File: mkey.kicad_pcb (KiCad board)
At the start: 2 copper layers, 1 part, among them U1 ESP32-S3-WROOM-2

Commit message: Initial KLE import of layout, need to add stabs and other sized keys
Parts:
- added BOOT_SW1: SW_Push, Connector_USB:USB_C_Receptacle_HRO_TYPE-C-31-M-12, F.Cu at (336.1, -28.6)
- added C1: 1uF 16V, Capacitor_SMD:C_0402_1005Metric, F.Cu at (346.3, -33.4)
- added C2: 10uF 16V, Capacitor_SMD:C_0805_2012Metric, F.Cu at (346.3, -31.4)
- added C3: 22pF 50V, Capacitor_SMD:C_0603_1608Metric, F.Cu at (346.3, -29.5)
- added C4: 10uF 16V, Capacitor_SMD:C_0805_2012Metric, F.Cu at (346.3, -27.5)
- added C5: 1uF 16V, Capacitor_SMD:C_0402_1005Metric, F.Cu at (350.0, -22.6)
- added C6: 100nF 10V, Capacitor_SMD:C_0402_1005Metric, F.Cu at (355.9, -23.9)
- added C7: 10nF 10V, Capacitor_SMD:C_0402_1005Metric, F.Cu at (350.0, -19.6)
- added C8: 1nF 10V, Capacitor_SMD:C_0402_1005Metric, F.Cu at (346.3, -25.5)
- added D1: D_Small, Diode_SMD:D_SOD-123, F.Cu at (50.0, 59.5)
- added D10: D_Small, Diode_SMD:D_SOD-123, F.Cu at (221.5, 59.5)
- added D11: D_Small, Diode_SMD:D_SOD-123, F.Cu at (240.5, 59.5)
- added D12: D_Small, Diode_SMD:D_SOD-123, F.Cu at (259.6, 59.5)
- added D13: D_Small, Diode_SMD:D_SOD-123, F.Cu at (278.6, 59.5)
- added D14: D_Small, Diode_SMD:D_SOD-123, F.Cu at (307.2, 59.5)
- added D15: D_Small, Diode_SMD:D_SOD-123, F.Cu at (54.8, 78.5)
- added D16: D_Small, Diode_SMD:D_SOD-123, F.Cu at (78.6, 78.5)
- added D17: D_Small, Diode_SMD:D_SOD-123, F.Cu at (97.6, 78.5)
- added D18: D_Small, Diode_SMD:D_SOD-123, F.Cu at (116.7, 78.5)
- added D19: D_Small, Diode_SMD:D_SOD-123, F.Cu at (135.7, 78.5)
- added D2: D_Small, Diode_SMD:D_SOD-123, F.Cu at (69.1, 59.5)
- added D20: D_Small, Diode_SMD:D_SOD-123, F.Cu at (154.8, 78.5)
- added D21: D_Small, Diode_SMD:D_SOD-123, F.Cu at (173.8, 78.5)
- added D22: D_Small, Diode_SMD:D_SOD-123, F.Cu at (192.9, 78.5)
- added D23: D_Small, Diode_SMD:D_SOD-123, F.Cu at (211.9, 78.5)
- added D24: D_Small, Diode_SMD:D_SOD-123, F.Cu at (231.0, 78.5)
- added D25: D_Small, Diode_SMD:D_SOD-123, F.Cu at (250.0, 78.5)
- added D26: D_Small, Diode_SMD:D_SOD-123, F.Cu at (269.1, 78.5)
- added D27: D_Small, Diode_SMD:D_SOD-123, F.Cu at (288.1, 78.5)
- added D28: D_Small, Diode_SMD:D_SOD-123, F.Cu at (314.3, 88.0)
- added D29: D_Small, Diode_SMD:D_SOD-123, F.Cu at (57.1, 97.6)
- added D3: D_Small, Diode_SMD:D_SOD-123, F.Cu at (88.1, 59.5)
- added D30: D_Small, Diode_SMD:D_SOD-123, F.Cu at (83.3, 97.6)
- added D31: D_Small, Diode_SMD:D_SOD-123, F.Cu at (102.4, 97.6)
- added D32: D_Small, Diode_SMD:D_SOD-123, F.Cu at (121.4, 97.6)
- added D33: D_Small, Diode_SMD:D_SOD-123, F.Cu at (140.5, 97.6)
- added D34: D_Small, Diode_SMD:D_SOD-123, F.Cu at (159.5, 97.6)
- added D35: D_Small, Diode_SMD:D_SOD-123, F.Cu at (178.6, 97.6)
- added D36: D_Small, Diode_SMD:D_SOD-123, F.Cu at (197.6, 97.6)
- added D37: D_Small, Diode_SMD:D_SOD-123, F.Cu at (216.7, 97.6)
- added D38: D_Small, Diode_SMD:D_SOD-123, F.Cu at (235.7, 97.6)
- added D39: D_Small, Diode_SMD:D_SOD-123, F.Cu at (254.8, 97.6)
- added D4: D_Small, Diode_SMD:D_SOD-123, F.Cu at (107.2, 59.5)
- added D40: D_Small, Diode_SMD:D_SOD-123, F.Cu at (273.8, 97.6)
- added D41: D_Small, Diode_SMD:D_SOD-123, F.Cu at (292.9, 97.6)
- added D42: D_Small, Diode_SMD:D_SOD-123, F.Cu at (52.4, 116.6)
- added D43: D_Small, Diode_SMD:D_SOD-123, F.Cu at (73.8, 116.6)
- added D44: D_Small, Diode_SMD:D_SOD-123, F.Cu at (92.9, 116.6)
- added D45: D_Small, Diode_SMD:D_SOD-123, F.Cu at (111.9, 116.6)
- added D46: D_Small, Diode_SMD:D_SOD-123, F.Cu at (131.0, 116.6)
- added D47: D_Small, Diode_SMD:D_SOD-123, F.Cu at (150.0, 116.6)
- added D48: D_Small, Diode_SMD:D_SOD-123, F.Cu at (169.1, 116.6)
- added D49: D_Small, Diode_SMD:D_SOD-123, F.Cu at (188.1, 116.6)
- added D5: D_Small, Diode_SMD:D_SOD-123, F.Cu at (126.2, 59.5)
- added D50: D_Small, Diode_SMD:D_SOD-123, F.Cu at (207.2, 116.6)
- added D51: D_Small, Diode_SMD:D_SOD-123, F.Cu at (226.2, 116.6)
- added D52: D_Small, Diode_SMD:D_SOD-123, F.Cu at (245.3, 116.6)
- added D53: D_Small, Diode_SMD:D_SOD-123, F.Cu at (264.3, 116.6)
- added D54: D_Small, Diode_SMD:D_SOD-123, F.Cu at (300.0, 116.6)
- added D55: D_Small, Diode_SMD:D_SOD-123, F.Cu at (359.6, 116.6)
- added D56: D_Small, Diode_SMD:D_SOD-123, F.Cu at (52.4, 135.7)
- added D57: D_Small, Diode_SMD:D_SOD-123, F.Cu at (76.2, 135.7)
- added D58: D_Small, Diode_SMD:D_SOD-123, F.Cu at (100.0, 135.7)
- added D59: D_Small, Diode_SMD:D_SOD-123, F.Cu at (171.4, 135.7)
- added D6: D_Small, Diode_SMD:D_SOD-123, F.Cu at (145.3, 59.5)
- added D60: D_Small, Diode_SMD:D_SOD-123, F.Cu at (242.9, 135.7)
- added D61: D_Small, Diode_SMD:D_SOD-123, F.Cu at (266.7, 135.7)
- added D62: D_Small, Diode_SMD:D_SOD-123, F.Cu at (290.5, 135.7)
- added D63: D_Small, Diode_SMD:D_SOD-123, F.Cu at (314.3, 135.7)
- added D64: D_Small, Diode_SMD:D_SOD-123, F.Cu at (340.5, 135.7)
- added D65: D_Small, Diode_SMD:D_SOD-123, F.Cu at (359.6, 135.7)
- added D66: D_Small, Diode_SMD:D_SOD-123, F.Cu at (378.6, 135.7)
- added D67: B5819W, Diode_SMD:D_SOD-123, F.Cu at (362.2, -56.2)
- added D68: PESD3V3L1BA,115, Diode_SMD:D_SOD-323, F.Cu at (362.2, -52.8)
- added D69: SP0503BAHT, Package_TO_SOT_SMD:SOT-143, B.Cu at (276.2, 60.0)
- added D7: D_Small, Diode_SMD:D_SOD-123, F.Cu at (164.3, 59.5)
- added D8: D_Small, Diode_SMD:D_SOD-123, F.Cu at (183.4, 59.5)
- added D9: D_Small, Diode_SMD:D_SOD-123, F.Cu at (202.4, 59.5)
- added J1: USB_C_REP_2.0, Connector_USB:USB_C_Receptacle_HRO_TYPE-C-31-M-12, F.Cu at (336.1, -18.1)
- added L1: SPH4018H2R2MT (2.2uH 2.2A), Inductor_SMD:L_Bourns-SRN4018, F.Cu at (350.8, -26.9)
- added MX1: MX_SW_solder, PCM_marbastlib-mx:SW_MX_1u, F.Cu at (46.8, 58.7)
- added MX10: MX_SW_solder, PCM_marbastlib-mx:SW_MX_1u, F.Cu at (218.3, 58.7)
- added MX11: MX_SW_solder, PCM_marbastlib-mx:SW_MX_1u, F.Cu at (237.3, 58.7)
- added MX12: MX_SW_solder, PCM_marbastlib-mx:SW_MX_1u, F.Cu at (256.4, 58.7)
- added MX13: MX_SW_solder, PCM_marbastlib-mx:SW_MX_1u, F.Cu at (275.4, 58.7)
- added MX14: MX_SW_solder, PCM_marbastlib-mx:SW_MX_1u, F.Cu at (304.0, 58.7)
- added MX15: MX_SW_solder, PCM_marbastlib-mx:SW_MX_1u, F.Cu at (51.6, 77.7)
- added MX16: MX_SW_solder, PCM_marbastlib-mx:SW_MX_1u, F.Cu at (75.4, 77.7)
- added MX17: MX_SW_solder, PCM_marbastlib-mx:SW_MX_1u, F.Cu at (94.5, 77.7)
- added MX18: MX_SW_solder, PCM_marbastlib-mx:SW_MX_1u, F.Cu at (113.5, 77.7)
- added MX19: MX_SW_solder, PCM_marbastlib-mx:SW_MX_1u, F.Cu at (132.6, 77.7)
- added MX2: MX_SW_solder, PCM_marbastlib-mx:SW_MX_1u, F.Cu at (65.9, 58.7)
- added MX20: MX_SW_solder, PCM_marbastlib-mx:SW_MX_1u, F.Cu at (151.6, 77.7)
- added MX21: MX_SW_solder, PCM_marbastlib-mx:SW_MX_1u, F.Cu at (170.7, 77.7)
- added MX22: MX_SW_solder, PCM_marbastlib-mx:SW_MX_1u, F.Cu at (189.7, 77.7)
- added MX23: MX_SW_solder, PCM_marbastlib-mx:SW_MX_1u, F.Cu at (208.8, 77.7)
- added MX24: MX_SW_solder, PCM_marbastlib-mx:SW_MX_1u, F.Cu at (227.8, 77.7)
- added MX25: MX_SW_solder, PCM_marbastlib-mx:SW_MX_1u, F.Cu at (246.9, 77.7)
- added MX26: MX_SW_solder, PCM_marbastlib-mx:SW_MX_1u, F.Cu at (265.9, 77.7)
- added MX27: MX_SW_solder, PCM_marbastlib-mx:SW_MX_1u, F.Cu at (285.0, 77.7)
- added MX28: MX_SW_solder, PCM_marbastlib-mx:SW_MX_1u, F.Cu at (311.1, 87.2)
- added MX29: MX_SW_solder, PCM_marbastlib-mx:SW_MX_1u, F.Cu at (54.0, 96.8)
- added MX3: MX_SW_solder, PCM_marbastlib-mx:SW_MX_1u, F.Cu at (84.9, 58.7)
- added MX30: MX_SW_solder, PCM_marbastlib-mx:SW_MX_1u, F.Cu at (80.2, 96.8)
- added MX31: MX_SW_solder, PCM_marbastlib-mx:SW_MX_1u, F.Cu at (99.2, 96.8)
- added MX32: MX_SW_solder, PCM_marbastlib-mx:SW_MX_1u, F.Cu at (118.3, 96.8)
- added MX33: MX_SW_solder, PCM_marbastlib-mx:SW_MX_1u, F.Cu at (137.3, 96.8)
- added MX34: MX_SW_solder, PCM_marbastlib-mx:SW_MX_1u, F.Cu at (156.4, 96.8)
- added MX35: MX_SW_solder, PCM_marbastlib-mx:SW_MX_1u, F.Cu at (175.4, 96.8)
- added MX36: MX_SW_solder, PCM_marbastlib-mx:SW_MX_1u, F.Cu at (194.5, 96.8)
- added MX37: MX_SW_solder, PCM_marbastlib-mx:SW_MX_1u, F.Cu at (213.5, 96.8)
- added MX38: MX_SW_solder, PCM_marbastlib-mx:SW_MX_1u, F.Cu at (232.6, 96.8)
- added MX39: MX_SW_solder, PCM_marbastlib-mx:SW_MX_1u, F.Cu at (251.6, 96.8)
- added MX4: MX_SW_solder, PCM_marbastlib-mx:SW_MX_1u, F.Cu at (104.0, 58.7)
- added MX40: MX_SW_solder, PCM_marbastlib-mx:SW_MX_1u, F.Cu at (270.7, 96.8)
- added MX41: MX_SW_solder, PCM_marbastlib-mx:SW_MX_1u, F.Cu at (289.7, 96.8)
- added MX42: MX_SW_solder, PCM_marbastlib-mx:SW_MX_1u, F.Cu at (49.2, 115.8)
- added MX43: MX_SW_solder, PCM_marbastlib-mx:SW_MX_1u, F.Cu at (70.6, 115.8)
- added MX44: MX_SW_solder, PCM_marbastlib-mx:SW_MX_1u, F.Cu at (89.7, 115.8)
- added MX45: MX_SW_solder, PCM_marbastlib-mx:SW_MX_1u, F.Cu at (108.7, 115.8)
- added MX46: MX_SW_solder, PCM_marbastlib-mx:SW_MX_1u, F.Cu at (127.8, 115.8)
- added MX47: MX_SW_solder, PCM_marbastlib-mx:SW_MX_1u, F.Cu at (146.8, 115.8)
- added MX48: MX_SW_solder, PCM_marbastlib-mx:SW_MX_1u, F.Cu at (165.9, 115.8)
- added MX49: MX_SW_solder, PCM_marbastlib-mx:SW_MX_1u, F.Cu at (184.9, 115.8)
- added MX5: MX_SW_solder, PCM_marbastlib-mx:SW_MX_1u, F.Cu at (123.0, 58.7)
- added MX50: MX_SW_solder, PCM_marbastlib-mx:SW_MX_1u, F.Cu at (204.0, 115.8)
- added MX51: MX_SW_solder, PCM_marbastlib-mx:SW_MX_1u, F.Cu at (223.0, 115.8)
- added MX52: MX_SW_solder, PCM_marbastlib-mx:SW_MX_1u, F.Cu at (242.1, 115.8)
- added MX53: MX_SW_solder, PCM_marbastlib-mx:SW_MX_1u, F.Cu at (261.1, 115.8)
- added MX54: MX_SW_solder, PCM_marbastlib-mx:SW_MX_1u, F.Cu at (296.9, 115.8)
- added MX55: MX_SW_solder, PCM_marbastlib-mx:SW_MX_1u, F.Cu at (356.4, 115.8)
- added MX56: MX_SW_solder, PCM_marbastlib-mx:SW_MX_1u, F.Cu at (49.2, 134.9)
- added MX57: MX_SW_solder, PCM_marbastlib-mx:SW_MX_1u, F.Cu at (73.0, 134.9)
- added MX58: MX_SW_solder, PCM_marbastlib-mx:SW_MX_1u, F.Cu at (96.8, 134.9)
- added MX59: MX_SW_solder, PCM_marbastlib-mx:SW_MX_1u, F.Cu at (168.3, 134.9)
- added MX6: MX_SW_solder, PCM_marbastlib-mx:SW_MX_1u, F.Cu at (142.1, 58.7)
- added MX60: MX_SW_solder, PCM_marbastlib-mx:SW_MX_1u, F.Cu at (239.7, 134.9)
- added MX61: MX_SW_solder, PCM_marbastlib-mx:SW_MX_1u, F.Cu at (263.5, 134.9)
- added MX62: MX_SW_solder, PCM_marbastlib-mx:SW_MX_1u, F.Cu at (287.3, 134.9)
- added MX63: MX_SW_solder, PCM_marbastlib-mx:SW_MX_1u, F.Cu at (311.1, 134.9)
- added MX64: MX_SW_solder, PCM_marbastlib-mx:SW_MX_1u, F.Cu at (337.3, 134.9)
- added MX65: MX_SW_solder, PCM_marbastlib-mx:SW_MX_1u, F.Cu at (356.4, 134.9)
- added MX66: MX_SW_solder, PCM_marbastlib-mx:SW_MX_1u, F.Cu at (375.4, 134.9)
- added MX7: MX_SW_solder, PCM_marbastlib-mx:SW_MX_1u, F.Cu at (161.1, 58.7)
- added MX8: MX_SW_solder, PCM_marbastlib-mx:SW_MX_1u, F.Cu at (180.2, 58.7)
- added MX9: MX_SW_solder, PCM_marbastlib-mx:SW_MX_1u, F.Cu at (199.2, 58.7)
- added R1: 10kR 1%, Resistor_SMD:R_0402_1005Metric, F.Cu at (343.4, -33.4)
- added R2: 10kR 1%, Resistor_SMD:R_0402_1005Metric, F.Cu at (343.4, -31.4)
- added R3: 100kR 1%, Resistor_SMD:R_0402_1005Metric, F.Cu at (343.4, -29.4)
- added R4: 22k1R 1%, Resistor_SMD:R_0402_1005Metric, F.Cu at (343.4, -27.4)
- added R5: 5k1R 1%, Resistor_SMD:R_0402_1005Metric, F.Cu at (343.4, -25.4)
- added R6: 5k1R 1%, Resistor_SMD:R_0402_1005Metric, F.Cu at (343.4, -23.5)
- added R7: 10kR 1%, Resistor_SMD:R_0402_1005Metric, F.Cu at (343.4, -21.5)
- added R8: 0R 1%, Resistor_SMD:R_0402_1005Metric, F.Cu at (343.4, -19.5)
- added RESET_SW1: SW_Push, Button_Switch_SMD:SW_SPST_PTS810, F.Cu at (351.1, -32.0)
- added U2: SY8088, Package_TO_SOT_SMD:SOT-23-5, F.Cu at (350.3, -15.9)
- U1: value ESP32-S3-WROOM-2 -> ESP32-S3-WROOM-1; footprint PCM_Espressif:ESP32-S3-WROOM-2 -> PCM_Espressif:ESP32-S3-WROOM-1; moved to B.Cu
- moved U1 354.9 mm to (384.3, -46.0), turned to 180 degrees
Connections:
- net Net-(U1-GND-Pad1) renamed GND
- U1 pad 13: unconnected-(U1-GPIO19/U1RTS/ADC2_CH8/CLK_OUT2/USB_D--Pad13) -> USB_D-
- U1 pad 14: unconnected-(U1-GPIO20/U1CTS/ADC2_CH9/CLK_OUT1/USB_D+-Pad14) -> USB_D+
- U1 pad 2: unconnected-(U1-3V3-Pad2) -> CHIP_POWER
- U1 pad 27: unconnected-(U1-GPIO0/BOOT-Pad27) -> BOOT
- U1 pad 3: unconnected-(U1-EN-Pad3) -> CHIP_PU

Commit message: flipped diodes and smd's to back layer
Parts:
- BOOT_SW1: footprint Connector_USB:USB_C_Receptacle_HRO_TYPE-C-31-M-12 -> Button_Switch_SMD:SW_SPST_PTS810; moved to B.Cu
- C1, C2, C3, C4, C5, C6, C7, C8, D1, D10, D11, D12, D13, D14, D15, D16, D17, D18, D19, D2, D20, D21, D22, D23, D24, D25, D26, D27, D28, D29, D3, D30, D31, D32, D33, D34, D35, D36, D37, D38, D39, D4, D40, D41, D42, D43, D44, D45, D46, D47, D48, D49, D5, D50, D51, D52, D53, D54, D55, D56, D57, D58, D59, D6, D60, D61, D62, D63, D64, D65, D66, D67, D68, D7, D8, D9, J1, L1, R1, R2, R3, R4, R5, R6, R7, R8, RESET_SW1, U2: moved to B.Cu
- MX15: footprint PCM_marbastlib-mx:SW_MX_1u -> PCM_marbastlib-mx:SW_MX_1.5u
- MX29: footprint PCM_marbastlib-mx:SW_MX_1u -> PCM_marbastlib-mx:SW_MX_1.75u
- MX42, MX56, MX57, MX58, MX60, MX61, MX62, MX63: footprint PCM_marbastlib-mx:SW_MX_1u -> PCM_marbastlib-mx:SW_MX_1.25u
- moved BOOT_SW1 100.0 mm to (398.5, 49.7), turned to 180 degrees
- moved J1 100.0 mm to (398.5, 60.1), turned to 180 degrees
- moved R1 91.7 mm to (391.2, 44.9), turned to 180 degrees
- moved R2 91.7 mm to (391.2, 46.9), turned to 180 degrees
- moved R3 91.7 mm to (391.2, 48.8), turned to 180 degrees
- moved R4 91.7 mm to (391.2, 50.8), turned to 180 degrees
- moved R5 91.7 mm to (391.2, 52.8), turned to 180 degrees
- moved R6 91.7 mm to (391.2, 54.8), turned to 180 degrees
- moved R7 91.7 mm to (391.2, 56.8), turned to 180 degrees
- moved R8 91.7 mm to (391.2, 58.8), turned to 180 degrees
- moved U1 91.2 mm to (340.4, 33.9)
- moved C1 88.8 mm to (388.3, 44.9), turned to 180 degrees
- moved C2 88.8 mm to (388.3, 46.8), turned to 180 degrees
- moved C3 88.8 mm to (388.3, 48.8), turned to 180 degrees
- moved C4 88.8 mm to (388.3, 50.8), turned to 180 degrees
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
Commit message: Added stabs
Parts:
- added S1: MX_stab, PCM_marbastlib-mx:STAB_MX_P_6.25u, F.Cu at (164.9, 130.8)
- added S2: MX_stab, PCM_marbastlib-mx:STAB_MX_P_2u, F.Cu at (300.7, 54.6)
- added S4: MX_stab, PCM_marbastlib-mx:STAB_MX_P_2.75u, F.Cu at (293.5, 111.7)
- added S5: MX_stab, PCM_marbastlib-mx:STAB_MX_ISO-ROT, F.Cu at (307.8, 83.2)
- moved D69 121.0 mm to (389.7, 24.6)

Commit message: small updates
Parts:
- moved J1 74.4 mm to (325.1, 47.9), turned to 0 degrees
- moved U1 53.4 mm to (365.6, 80.9), turned to 90 degrees
- moved D67 10.3 mm to (372.4, 32.4)
- moved D68 10.3 mm to (372.4, 35.8)
- moved D69 10.3 mm to (389.7, 34.9)

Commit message: switch out small comps, to 0603's, start draft routing
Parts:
- C1, C5, C6, C7, C8: footprint Capacitor_SMD:C_0402_1005Metric -> Capacitor_SMD:C_0603_1608Metric
- D69: moved to F.Cu
- R1, R2, R3, R4, R5, R6, R7, R8: footprint Resistor_SMD:R_0402_1005Metric -> Resistor_SMD:R_0603_1608Metric
- moved BOOT_SW1 80.3 mm to (331.8, 94.4)
- moved R7 74.7 mm to (330.2, 100.0), turned to -90 degrees
- moved C8 74.1 mm to (327.0, 94.4), turned to 90 degrees
- moved R1 43.0 mm to (349.5, 55.6)
- moved J1 40.4 mm to (365.5, 47.9)
- moved C1 36.2 mm to (352.4, 39.7)
- moved C5 36.0 mm to (348.7, 53.3), turned to 90 degrees
- moved U1 34.5 mm to (337.3, 61.1), turned to 180 degrees
- moved C4 34.4 mm to (356.4, 63.7), turned to -90 degrees
- moved R3 33.4 mm to (361.2, 63.5), turned to -90 degrees
- moved C7 33.2 mm to (351.9, 53.3), turned to 90 degrees
- moved C3 33.0 mm to (358.8, 63.5), turned to -90 degrees
- moved R4 28.9 mm to (365.1, 63.5), turned to 90 degrees
- moved C6 28.4 mm to (350.3, 53.3), turned to 90 degrees
- moved D69 27.8 mm to (365.3, 48.2), turned to 0 degrees
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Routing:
- net CHIP_POWER: track 0.00 -> 18.2 mm
- net Net-(U2-FB): track 0.00 -> 13.6 mm
- net VBUS: track 0.00 -> 5.75 mm
- net Net-(U2-EN): track 0.00 -> 5.51 mm
- net Net-(D67-A): track 0.00 -> 3.30 mm
- net /Buck_Coil: track 0.00 -> 2.77 mm
- net CHIP_PU: track 0.00 -> 2.63 mm
- added copper zone on B.Cu, net GND
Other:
- board outline added: 346.1 x 94.5 mm

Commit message: wire matrix, route some columns and rows, need to rewire some columns on the bottom row of keys to make routing easier
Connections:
- D1 pad 1: unconnected-(D1-K-Pad1) -> ROW0
- D10 pad 1: unconnected-(D10-K-Pad1) -> ROW0
- D11 pad 1: unconnected-(D11-K-Pad1) -> ROW0
- D12 pad 1: unconnected-(D12-K-Pad1) -> ROW0
- D13 pad 1: unconnected-(D13-K-Pad1) -> ROW0
- D14 pad 1: unconnected-(D14-K-Pad1) -> ROW0
- D15 pad 1: unconnected-(D15-K-Pad1) -> ROW1
- D16 pad 1: unconnected-(D16-K-Pad1) -> ROW1
- D17 pad 1: unconnected-(D17-K-Pad1) -> ROW1
- D18 pad 1: unconnected-(D18-K-Pad1) -> ROW1
- D19 pad 1: unconnected-(D19-K-Pad1) -> ROW1
- D2 pad 1: unconnected-(D2-K-Pad1) -> ROW0
- D20 pad 1: unconnected-(D20-K-Pad1) -> ROW1
- D21 pad 1: unconnected-(D21-K-Pad1) -> ROW1
- D22 pad 1: unconnected-(D22-K-Pad1) -> ROW1
- D23 pad 1: unconnected-(D23-K-Pad1) -> ROW1
- D24 pad 1: unconnected-(D24-K-Pad1) -> ROW1
- D25 pad 1: unconnected-(D25-K-Pad1) -> ROW1
- D26 pad 1: unconnected-(D26-K-Pad1) -> ROW1
- D27 pad 1: unconnected-(D27-K-Pad1) -> ROW1
- D28 pad 1: unconnected-(D28-K-Pad1) -> ROW1
- D29 pad 1: unconnected-(D29-K-Pad1) -> ROW2
- D3 pad 1: unconnected-(D3-K-Pad1) -> ROW0
- D30 pad 1: unconnected-(D30-K-Pad1) -> ROW2
- D31 pad 1: unconnected-(D31-K-Pad1) -> ROW2
- D32 pad 1: unconnected-(D32-K-Pad1) -> ROW2
- D33 pad 1: unconnected-(D33-K-Pad1) -> ROW2
- D34 pad 1: unconnected-(D34-K-Pad1) -> ROW2
- D35 pad 1: unconnected-(D35-K-Pad1) -> ROW2
- D36 pad 1: unconnected-(D36-K-Pad1) -> ROW2
- D37 pad 1: unconnected-(D37-K-Pad1) -> ROW2
- D38 pad 1: unconnected-(D38-K-Pad1) -> ROW2
- D39 pad 1: unconnected-(D39-K-Pad1) -> ROW2
- D4 pad 1: unconnected-(D4-K-Pad1) -> ROW0
- D40 pad 1: unconnected-(D40-K-Pad1) -> ROW2
- D41 pad 1: unconnected-(D41-K-Pad1) -> ROW2
- D42 pad 1: unconnected-(D42-K-Pad1) -> ROW3
- D43 pad 1: unconnected-(D43-K-Pad1) -> ROW3
- D44 pad 1: unconnected-(D44-K-Pad1) -> ROW3
- D45 pad 1: unconnected-(D45-K-Pad1) -> ROW3
- D46 pad 1: unconnected-(D46-K-Pad1) -> ROW3
- D47 pad 1: unconnected-(D47-K-Pad1) -> ROW3
- D48 pad 1: unconnected-(D48-K-Pad1) -> ROW3
- D49 pad 1: unconnected-(D49-K-Pad1) -> ROW3
- D5 pad 1: unconnected-(D5-K-Pad1) -> ROW0
- D50 pad 1: unconnected-(D50-K-Pad1) -> ROW3
- D51 pad 1: unconnected-(D51-K-Pad1) -> ROW3
- D52 pad 1: unconnected-(D52-K-Pad1) -> ROW3
- D53 pad 1: unconnected-(D53-K-Pad1) -> ROW3
- D54 pad 1: unconnected-(D54-K-Pad1) -> ROW3
- D55 pad 1: unconnected-(D55-K-Pad1) -> ROW3
- D56 pad 1: unconnected-(D56-K-Pad1) -> ROW4
- D57 pad 1: unconnected-(D57-K-Pad1) -> ROW4
- D58 pad 1: unconnected-(D58-K-Pad1) -> ROW4
- D59 pad 1: unconnected-(D59-K-Pad1) -> ROW4
- D6 pad 1: unconnected-(D6-K-Pad1) -> ROW0
- D60 pad 1: unconnected-(D60-K-Pad1) -> ROW4
- D61 pad 1: unconnected-(D61-K-Pad1) -> ROW4
- D62 pad 1: unconnected-(D62-K-Pad1) -> ROW4
- D63 pad 1: unconnected-(D63-K-Pad1) -> ROW4
- D64 pad 1: unconnected-(D64-K-Pad1) -> ROW4
- D65 pad 1: unconnected-(D65-K-Pad1) -> ROW4
- D66 pad 1: unconnected-(D66-K-Pad1) -> ROW4
- D7 pad 1: unconnected-(D7-K-Pad1) -> ROW0
- D8 pad 1: unconnected-(D8-K-Pad1) -> ROW0
- D9 pad 1: unconnected-(D9-K-Pad1) -> ROW0
- MX1 pad 1: unconnected-(MX1-Pad1) -> COL0
- MX10 pad 1: unconnected-(MX10-Pad1) -> COL9
- MX11 pad 1: unconnected-(MX11-Pad1) -> COL10
- MX12 pad 1: unconnected-(MX12-Pad1) -> COL11
- MX13 pad 1: unconnected-(MX13-Pad1) -> COL12
- MX14 pad 1: unconnected-(MX14-Pad1) -> COL13
- MX15 pad 1: unconnected-(MX15-Pad1) -> COL0
- MX16 pad 1: unconnected-(MX16-Pad1) -> COL1
- MX17 pad 1: unconnected-(MX17-Pad1) -> COL2
- MX18 pad 1: unconnected-(MX18-Pad1) -> COL3
- MX19 pad 1: unconnected-(MX19-Pad1) -> COL4
- MX2 pad 1: unconnected-(MX2-Pad1) -> COL1
- MX20 pad 1: unconnected-(MX20-Pad1) -> COL5
- MX21 pad 1: unconnected-(MX21-Pad1) -> COL6
- MX22 pad 1: unconnected-(MX22-Pad1) -> COL7
- MX23 pad 1: unconnected-(MX23-Pad1) -> COL8
- MX24 pad 1: unconnected-(MX24-Pad1) -> COL9
- MX25 pad 1: unconnected-(MX25-Pad1) -> COL10
- MX26 pad 1: unconnected-(MX26-Pad1) -> COL11
- MX27 pad 1: unconnected-(MX27-Pad1) -> COL12
- MX28 pad 1: unconnected-(MX28-Pad1) -> COL13
- MX29 pad 1: unconnected-(MX29-Pad1) -> COL0
- MX3 pad 1: unconnected-(MX3-Pad1) -> COL2
- MX30 pad 1: unconnected-(MX30-Pad1) -> COL1
- MX31 pad 1: unconnected-(MX31-Pad1) -> COL2
- MX32 pad 1: unconnected-(MX32-Pad1) -> COL3
- MX33 pad 1: unconnected-(MX33-Pad1) -> COL4
- MX34 pad 1: unconnected-(MX34-Pad1) -> COL5
- MX35 pad 1: unconnected-(MX35-Pad1) -> COL6
- MX36 pad 1: unconnected-(MX36-Pad1) -> COL7
- MX37 pad 1: unconnected-(MX37-Pad1) -> COL8
- MX38 pad 1: unconnected-(MX38-Pad1) -> COL9
- MX39 pad 1: unconnected-(MX39-Pad1) -> COL10
- MX4 pad 1: unconnected-(MX4-Pad1) -> COL3
- MX40 pad 1: unconnected-(MX40-Pad1) -> COL11
- MX41 pad 1: unconnected-(MX41-Pad1) -> COL12
- MX42 pad 1: unconnected-(MX42-Pad1) -> COL0
- MX43 pad 1: unconnected-(MX43-Pad1) -> COL1
- MX44 pad 1: unconnected-(MX44-Pad1) -> COL2
- MX45 pad 1: unconnected-(MX45-Pad1) -> COL3
- MX46 pad 1: unconnected-(MX46-Pad1) -> COL4
- MX47 pad 1: unconnected-(MX47-Pad1) -> COL5
- MX48 pad 1: unconnected-(MX48-Pad1) -> COL6
- MX49 pad 1: unconnected-(MX49-Pad1) -> COL7
- MX5 pad 1: unconnected-(MX5-Pad1) -> COL4
- MX50 pad 1: unconnected-(MX50-Pad1) -> COL8
- MX51 pad 1: unconnected-(MX51-Pad1) -> COL9
- MX52 pad 1: unconnected-(MX52-Pad1) -> COL10
- MX53 pad 1: unconnected-(MX53-Pad1) -> COL11
- MX54 pad 1: unconnected-(MX54-Pad1) -> COL12
- MX55 pad 1: unconnected-(MX55-Pad1) -> COL13
- MX56 pad 1: unconnected-(MX56-Pad1) -> COL0
- MX57 pad 1: unconnected-(MX57-Pad1) -> COL1
- MX58 pad 1: unconnected-(MX58-Pad1) -> COL2
- MX59 pad 1: unconnected-(MX59-Pad1) -> COL3
- MX6 pad 1: unconnected-(MX6-Pad1) -> COL5
- MX60 pad 1: unconnected-(MX60-Pad1) -> COL7
- MX61 pad 1: unconnected-(MX61-Pad1) -> COL8
- MX62 pad 1: unconnected-(MX62-Pad1) -> COL9
- MX63 pad 1: unconnected-(MX63-Pad1) -> COL10
- MX64 pad 1: unconnected-(MX64-Pad1) -> COL11
- MX65 pad 1: unconnected-(MX65-Pad1) -> COL12
- MX66 pad 1: unconnected-(MX66-Pad1) -> COL13
- MX7 pad 1: unconnected-(MX7-Pad1) -> COL6
- MX8 pad 1: unconnected-(MX8-Pad1) -> COL7
- MX9 pad 1: unconnected-(MX9-Pad1) -> COL8
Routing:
- net ROW4: track 0.00 -> 326.2 mm
- net ROW3: track 0.00 -> 307.2 mm
- net ROW1: track 0.00 -> 264.9 mm
- net ROW0: track 0.00 -> 257.4 mm
- net ROW2: track 0.00 -> 235.7 mm
- net COL13: track 0.00 -> 127.8 mm
- net COL2: track 0.00 -> 89.7 mm
- net COL1: track 0.00 -> 87.7 mm
- net COL0: track 0.00 -> 82.4 mm
- net COL11: track 0.00 -> 67.7 mm
- net COL5: track 0.00 -> 67.7 mm
- net COL7: track 0.00 -> 67.7 mm
- net COL10: track 0.00 -> 67.7 mm
- net COL9: track 0.00 -> 67.7 mm
- net COL4: track 0.00 -> 67.7 mm
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
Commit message: finish routing matrix, rework mcu routing and start TODO
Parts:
- BOOT_SW1, C2, C8, R7, RESET_SW1: moved to F.Cu
- moved BOOT_SW1 46.0 mm to (374.6, 77.8), turned to 0 degrees
- moved R7 45.8 mm to (368.3, 74.6)
- moved C8 44.5 mm to (368.3, 77.8)
- moved C1 18.1 mm to (349.4, 57.5), turned to 0 degrees
- moved RESET_SW1 11.8 mm to (374.6, 70.6), turned to 0 degrees
- moved C2 5.77 mm to (369.9, 70.6), turned to -90 degrees
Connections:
- MX59 pad 1: COL3 -> COL5
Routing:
- net COL11: track 67.7 -> 152.4 mm
- net COL10: track 67.7 -> 145.7 mm
- net COL9: track 67.7 -> 141.4 mm
- net COL7: track 67.7 -> 137.0 mm
- net COL12: track 66.0 -> 133.8 mm
- net COL8: track 67.7 -> 134.8 mm
- net COL5: track 67.7 -> 101.8 mm
- net CHIP_PU: track 2.63 -> 4.59 mm

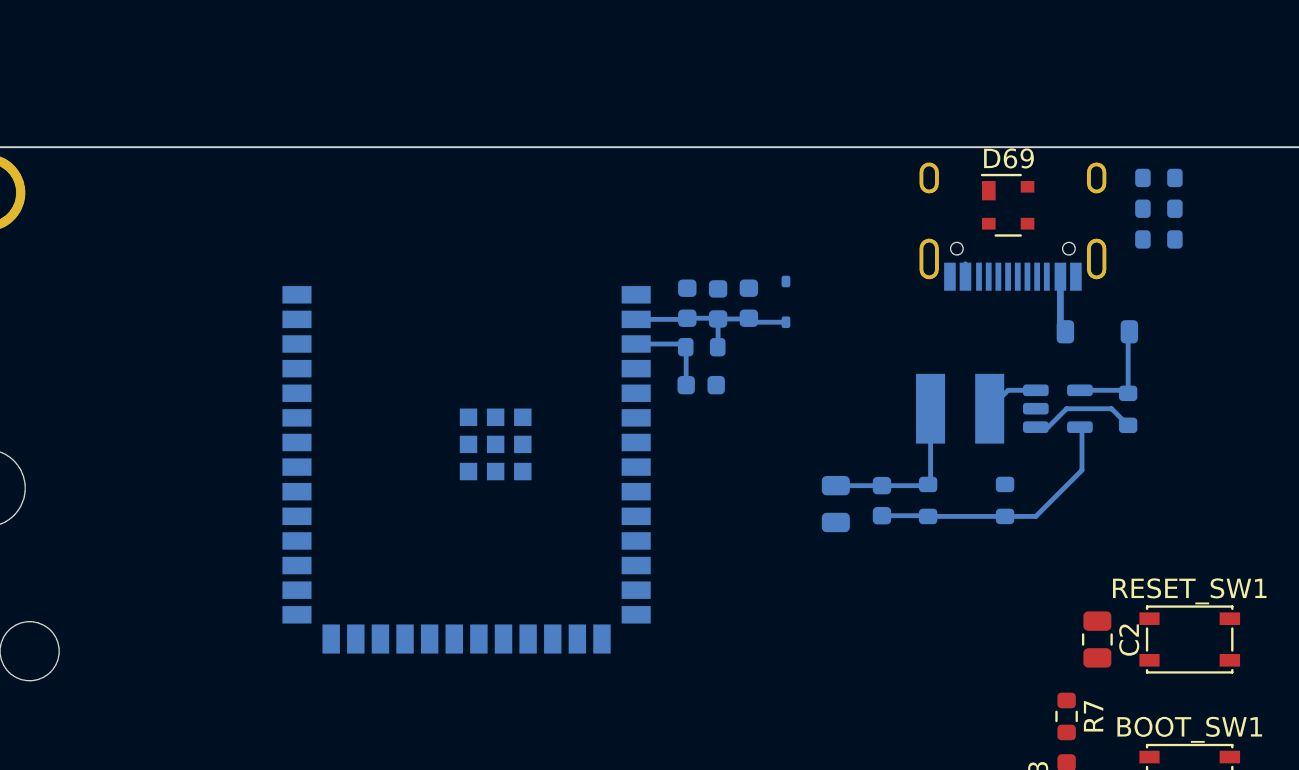
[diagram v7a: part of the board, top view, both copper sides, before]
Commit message: Flipped usb c and condensed the vcc filtering
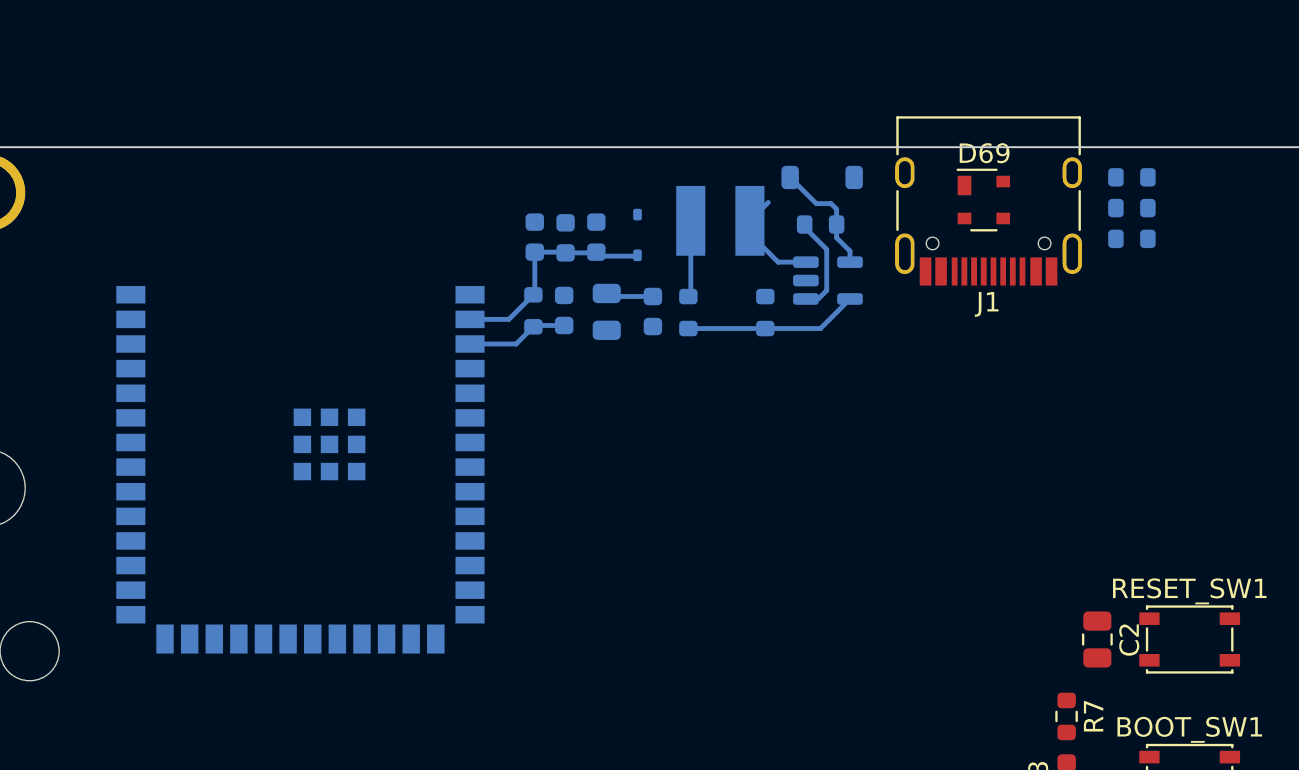
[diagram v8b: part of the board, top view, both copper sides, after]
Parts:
- J1: moved to F.Cu
- moved R2 18.5 mm to (355.6, 49.2), turned to 180 degrees
- moved D67 16.3 mm to (355.7, 46.8), turned to 0 degrees
- moved L1 15.7 mm to (350.4, 49.0)
- moved R3 15.7 mm to (348.8, 53.8)
- moved R4 15.7 mm to (352.8, 53.8)
- moved C4 15.4 mm to (344.6, 53.7)
- moved C3 15.3 mm to (347.0, 53.7)
- moved U2 13.6 mm to (356.0, 52.1)
- moved R1 8.89 mm to (340.8, 53.7), turned to -90 degrees
- moved C6 8.58 mm to (342.5, 49.9)
- moved C5 8.58 mm to (340.9, 49.9)
- moved C7 8.58 mm to (344.0, 49.9)
- moved U1 8.57 mm to (328.8, 61.1)
- moved D68 8.40 mm to (346.2, 49.8)
- moved C1 8.05 mm to (342.4, 53.7), turned to 90 degrees
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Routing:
- net Net-(U2-FB): track 13.6 -> 9.17 mm
- net Net-(D67-A): track 3.30 -> 0.00 mm
- net /Buck_Coil: track 2.77 -> 5.51 mm
- net CHIP_PU: track 4.59 -> 5.25 mm
